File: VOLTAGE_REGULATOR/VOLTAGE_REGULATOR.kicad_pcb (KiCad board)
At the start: 2 copper layers, 13 parts, among them J1 Screw_Terminal_01x02, J2 Screw_Terminal_01x02, J3 Screw_Terminal_01x02, U1 L7805, U2 L7809

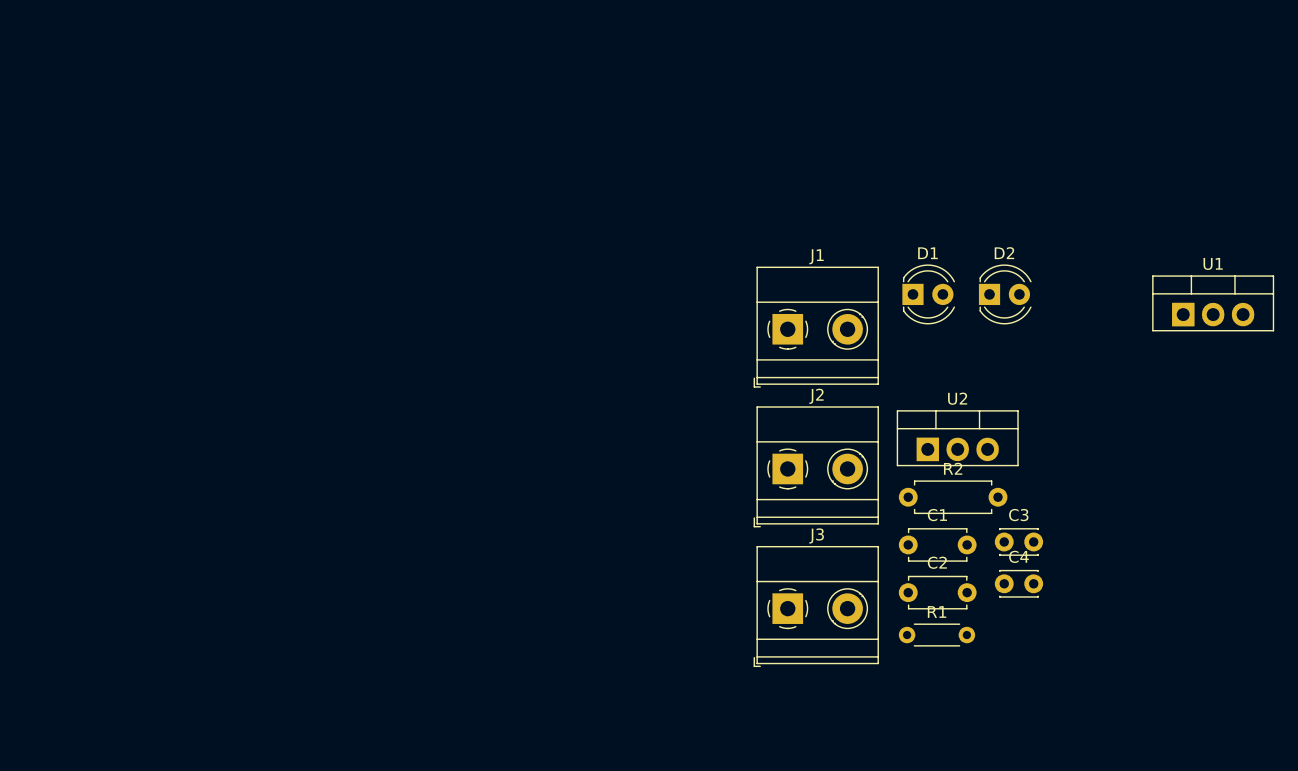
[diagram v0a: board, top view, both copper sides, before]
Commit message: voltage regulator: place components
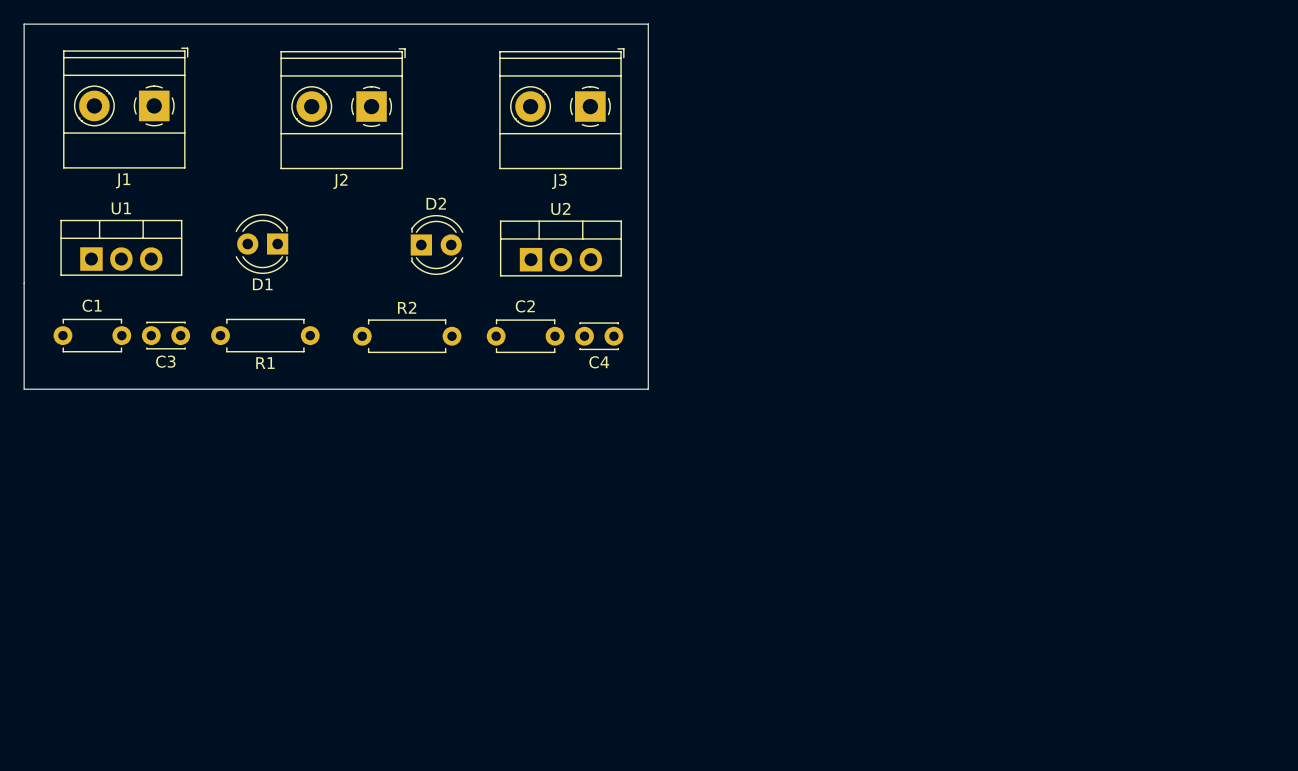
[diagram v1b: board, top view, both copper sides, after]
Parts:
- R1: footprint Resistor_THT:R_Axial_DIN0204_L3.6mm_D1.6mm_P5.08mm_Horizontal -> Resistor_THT:R_Axial_DIN0207_L6.3mm_D2.5mm_P7.62mm_Horizontal
- moved U1 92.8 mm to (92.7, 68.9)
- moved C1 73.9 mm to (90.3, 75.4)
- moved C3 72.1 mm to (100.3, 75.4), turned to 180 degrees
- moved J1 57.0 mm to (98.0, 55.9), turned to 180 degrees
- moved R1 56.7 mm to (111.3, 75.4), turned to 180 degrees
- moved D1 54.1 mm to (108.5, 67.7), turned to 180 degrees
- moved D2 48.4 mm to (120.7, 67.8)
- moved R2 48.3 mm to (115.7, 75.5)
- moved J2 46.9 mm to (116.5, 56.0), turned to 180 degrees
- moved J3 45.8 mm to (135.1, 56.0), turned to 180 degrees
- moved C2 41.2 mm to (127.1, 75.5)
- moved C4 39.2 mm to (137.1, 75.5), turned to 180 degrees
- moved U2 37.3 mm to (130.0, 69.0)
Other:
- board outline added: 53 x 31 mm

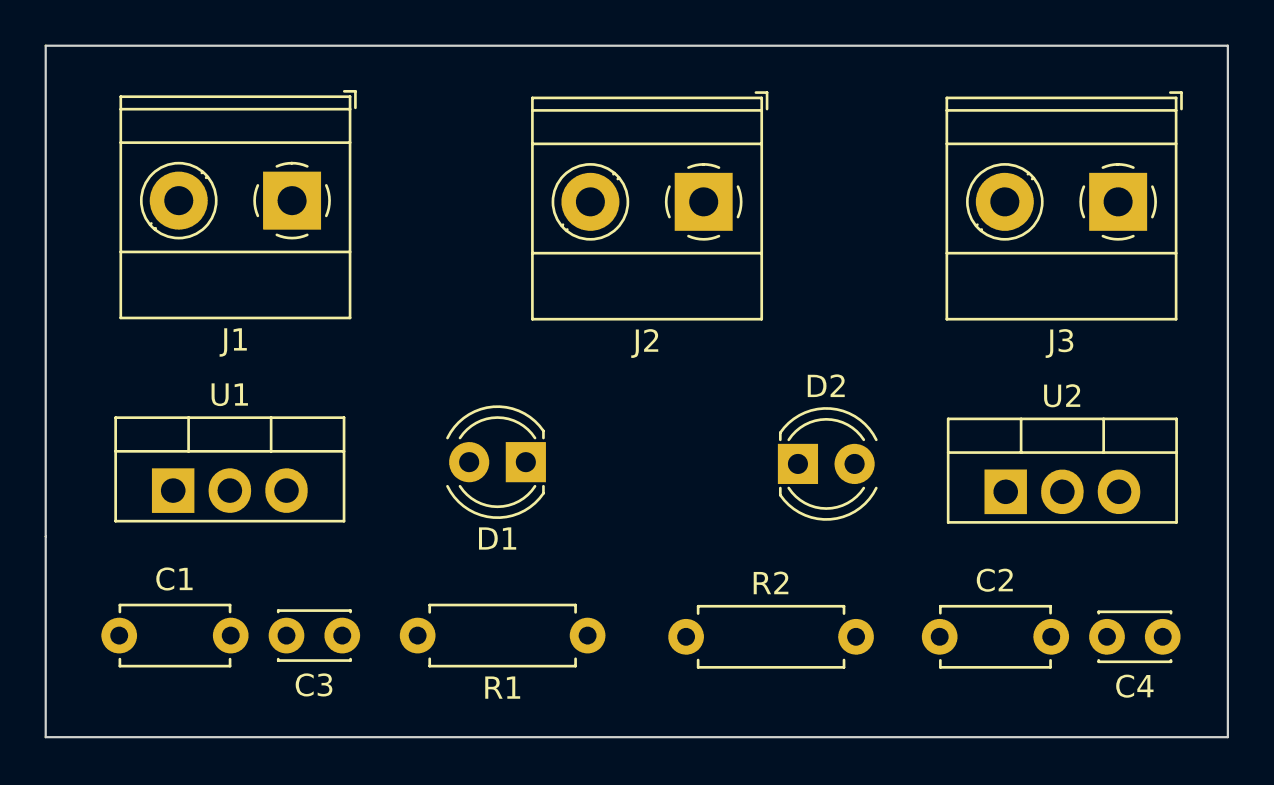
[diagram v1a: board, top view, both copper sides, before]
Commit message: route pcb main connections
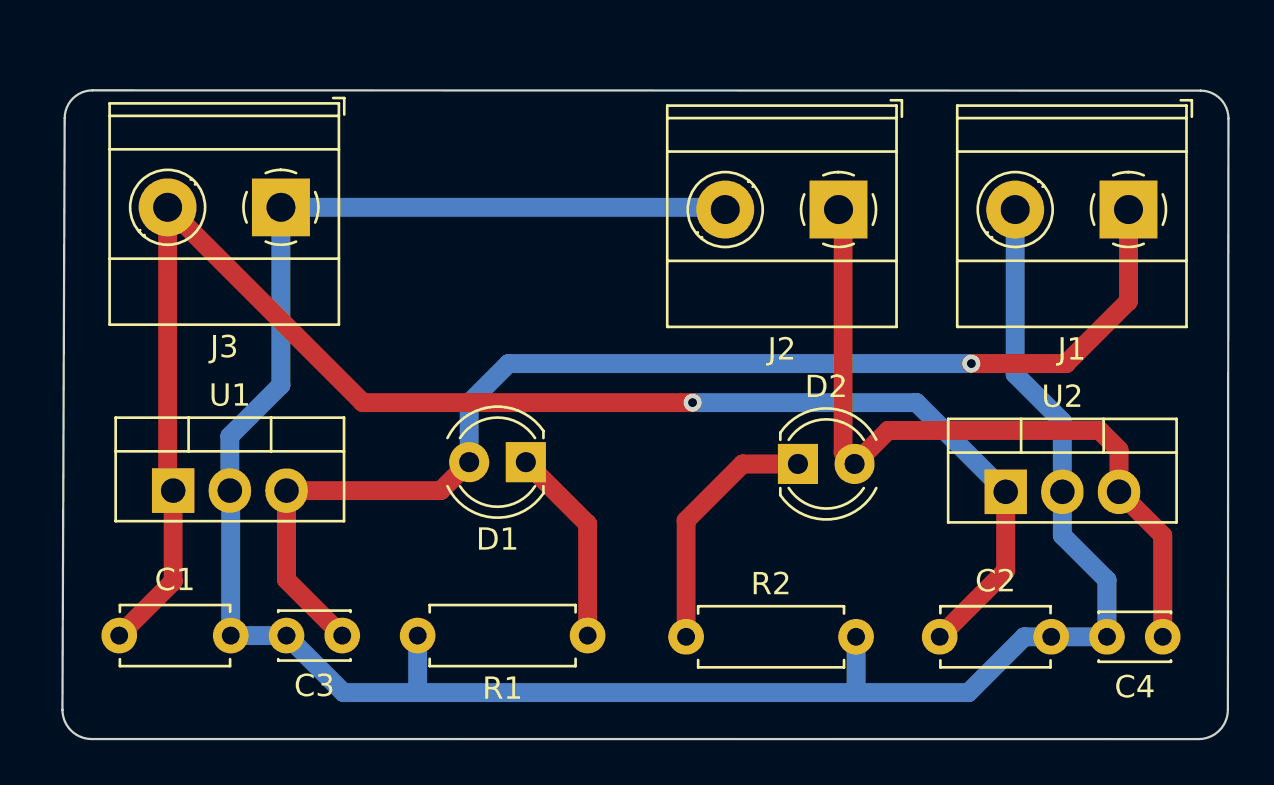
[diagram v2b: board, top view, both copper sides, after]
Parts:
- moved J3 37.5 mm to (97.5, 56.2)
- moved J1 37.5 mm to (135.5, 56.3)
- moved J2 6.05 mm to (122.5, 56.3)
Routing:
- net GND: track 0.00 -> 107.6 mm
- net +12V: track 0.00 -> 70.9 mm, vias 0 -> 1
- net /+5V_OUT: track 0.00 -> 54.5 mm, vias 0 -> 1
- net /+9V_OUT: track 0.00 -> 33.7 mm
- net Net-(D2-K): track 0.00 -> 11.3 mm
- net Net-(D1-K): track 0.00 -> 8.92 mm
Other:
- board size 53 x 31 mm -> 52.3 x 29.1 mm
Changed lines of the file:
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@@
   )
   (footprint "TerminalBlock_Phoenix:TerminalBlock_Phoenix_MKDS-1,5-2-5.08_1x02_P5.08mm_Horizontal" (layer "F.Cu")
-    (at 98.045 55.945 180)
+    (at 135.545 56.345 180)
     (descr "Terminal Block Phoenix MKDS-1,5-2-5.08, 2 pins, pitch 5.08mm, size 10.2x9.8mm^2, drill diamater 1.3mm, pad diameter 2.6mm, see http://www.farnell.com/datasheets/100425.pdf, script-generated using https://github.com/pointhi/kicad-footprint-generator/scripts/TerminalBlock_Phoenix")
     (tags "THT Terminal Block Phoenix MKDS-1,5-2-5.08 pitch 5.08mm size 10.2x9.8mm^2 drill 1.3mm pad 2.6mm")
@@
   )
   (footprint "TerminalBlock_Phoenix:TerminalBlock_Phoenix_MKDS-1,5-2-5.08_1x02_P5.08mm_Horizontal" (layer "F.Cu")
-    (at 135.08 56 180)
+    (at 97.545 56.245 180)
     (descr "Terminal Block Phoenix MKDS-1,5-2-5.08, 2 pins, pitch 5.08mm, size 10.2x9.8mm^2, drill diamater 1.3mm, pad diameter 2.6mm, see http://www.farnell.com/datasheets/100425.pdf, script-generated using https://github.com/pointhi/kicad-footprint-generator/scripts/TerminalBlock_Phoenix")
     (tags "THT Terminal Block Phoenix MKDS-1,5-2-5.08 pitch 5.08mm size 10.2x9.8mm^2 drill 1.3mm pad 2.6mm")
@@
   )
   (footprint "TerminalBlock_Phoenix:TerminalBlock_Phoenix_MKDS-1,5-2-5.08_1x02_P5.08mm_Horizontal" (layer "F.Cu")
-    (at 116.5 56 180)
+    (at 122.545 56.345 180)
     (descr "Terminal Block Phoenix MKDS-1,5-2-5.08, 2 pins, pitch 5.08mm, size 10.2x9.8mm^2, drill diamater 1.3mm, pad diameter 2.6mm, see http://www.farnell.com/datasheets/100425.pdf, script-generated using https://github.com/pointhi/kicad-footprint-generator/scripts/TerminalBlock_Phoenix")
     (tags "THT Terminal Block Phoenix MKDS-1,5-2-5.08 pitch 5.08mm size 10.2x9.8mm^2 drill 1.3mm pad 2.6mm")
@@
     )
   )
-  (gr_line (start 140 49) (end 140 80)
+  (gr_arc (start 138.776117 51.013883) (mid 139.66 51.38) (end 140.026117 52.263883)
     (stroke (width 0.1) (type default)) (layer "Edge.Cuts"))
-  (gr_line (start 140 80) (end 87 80)
+  (gr_line (start 138.776117 51.013883) (end 89.1 51)
     (stroke (width 0.1) (type default)) (layer "Edge.Cuts"))
-  (gr_line (start 87 80) (end 87 71)
+  (gr_line (start 87.85 52.25) (end 87.75 78.772888)
     (stroke (width 0.1) (type default)) (layer "Edge.Cuts"))
-  (gr_line (start 87 49) (end 140 49)
+  (gr_arc (start 89.061134 80.084022) (mid 88.134022 79.7) (end 87.75 78.772888)
     (stroke (width 0.1) (type default)) (layer "Edge.Cuts"))
-  (gr_line (start 87 71) (end 87 49)
+  (gr_line (start 89.061134 80.084022) (end 138.688866 80.086134)
     (stroke (width 0.1) (type default)) (layer "Edge.Cuts"))
+  (gr_arc (start 87.85 52.25) (mid 88.216117 51.366117) (end 89.1 51)
+    (stroke (width 0.1) (type default)) (layer "Edge.Cuts"))
+  (gr_arc (start 140.000034 78.775) (mid 139.616 79.702124) (end 138.688866 80.086134)
+    (stroke (width 0.1) (type default)) (layer "Edge.Cuts"))
+  (gr_line (start 140.000034 78.775) (end 140.026117 52.263883)
+    (stroke (width 0.1) (type default)) (layer "Edge.Cuts"))
+  (segment (start 92.465 56.245) (end 101.22 65) (width 0.85) (layer "F.Cu") (net 1))
+  (segment (start 92.715 68.945) (end 92.715 73.025) (width 0.85) (layer "F.Cu") (net 1))
+  (segment (start 101.22 65) (end 116 65) (width 0.85) (layer "F.Cu") (net 1))
+  (segment (start 92.715 73.025) (end 90.295 75.445) (width 0.85) (layer "F.Cu") (net 1))
+  (segment (start 130.04 72.54) (end 127.08 75.5) (width 0.85) (layer "F.Cu") (net 1))
+  (segment (start 92.465 68.695) (end 92.715 68.945) (width 0.85) (layer "F.Cu") (net 1))
+  (segment (start 92.465 56.245) (end 92.465 68.695) (width 0.85) (layer "F.Cu") (net 1))
+  (segment (start 130.04 69) (end 130.04 72.54) (width 0.85) (layer "F.Cu") (net 1))
+  (via (at 116 65) (size 0.8) (drill 0.4) (layers "F.Cu" "B.Cu") (net 1))
+  (segment (start 116 65) (end 126.04 65) (width 0.85) (layer "B.Cu") (net 1))
+  (segment (start 126.04 65) (end 130.04 69) (width 0.85) (layer "B.Cu") (net 1))
+  (segment (start 97.545 64.215) (end 97.545 56.245) (width 0.85) (layer "B.Cu") (net 2))
+  (segment (start 130.875 75.5) (end 128.375 78) (width 0.85) (layer "B.Cu") (net 2))
+  (segment (start 134.58 75.5) (end 132.08 75.5) (width 0.85) (layer "B.Cu") (net 2))
+  (segment (start 97.795 75.445) (end 95.295 75.445) (width 0.85) (layer "B.Cu") (net 2))
+  (segment (start 123.33 75.5) (end 123.33 77.795) (width 0.85) (layer "B.Cu") (net 2))
+  (segment (start 95.255 68.945) (end 95.255 66.505) (width 0.85) (layer "B.Cu") (net 2))
+  (segment (start 103.675 77.8) (end 103.875 78) (width 0.85) (layer "B.Cu") (net 2))
+  (segment (start 100.35 78) (end 97.795 75.445) (width 0.85) (layer "B.Cu") (net 2))
+  (segment (start 95.295 75.445) (end 95.295 68.985) (width 0.85) (layer "B.Cu") (net 2))
+  (segment (start 128.375 78) (end 123.125 78) (width 0.85) (layer "B.Cu") (net 2))
+  (segment (start 117.365 56.245) (end 117.465 56.345) (width 0.85) (layer "B.Cu") (net 2))
+  (segment (start 132.08 75.5) (end 130.875 75.5) (width 0.85) (layer "B.Cu") (net 2))
+  (segment (start 130.465 63.73) (end 130.465 56.345) (width 0.85) (layer "B.Cu") (net 2))
+  (segment (start 103.875 78) (end 100.35 78) (width 0.85) (layer "B.Cu") (net 2))
+  (segment (start 132.58 70.955) (end 134.58 72.955) (width 0.85) (layer "B.Cu") (net 2))
+  (segment (start 95.295 68.985) (end 95.255 68.945) (width 0.85) (layer "B.Cu") (net 2))
+  (segment (start 103.675 75.445) (end 103.675 77.8) (width 0.85) (layer "B.Cu") (net 2))
+  (segment (start 132.58 69) (end 132.58 70.955) (width 0.85) (layer "B.Cu") (net 2))
+  (segment (start 123.125 78) (end 103.875 78) (width 0.85) (layer "B.Cu") (net 2))
+  (segment (start 132.58 65.845) (end 132.58 69) (width 0.85) (layer "B.Cu") (net 2))
+  (segment (start 123.33 77.795) (end 123.125 78) (width 0.85) (layer "B.Cu") (net 2))
+  (segment (start 97.545 56.245) (end 117.365 56.245) (width 0.85) (layer "B.Cu") (net 2))
+  (segment (start 132.58 65.845) (end 130.465 63.73) (width 0.85) (layer "B.Cu") (net 2))
+  (segment (start 95.255 66.505) (end 97.545 64.215) (width 0.85) (layer "B.Cu") (net 2))
+  (segment (start 134.58 72.955) (end 134.58 75.5) (width 0.85) (layer "B.Cu") (net 2))
+  (segment (start 97.795 72.945) (end 100.295 75.445) (width 0.85) (layer "F.Cu") (net 3))
+  (segment (start 97.795 68.945) (end 104.71 68.945) (width 0.85) (layer "F.Cu") (net 3))
+  (segment (start 132.75 63.25) (end 135.545 60.455) (width 0.85) (layer "F.Cu") (net 3))
+  (segment (start 128.5 63.25) (end 132.75 63.25) (width 0.85) (layer "F.Cu") (net 3))
+  (segment (start 135.545 60.455) (end 135.545 56.345) (width 0.85) (layer "F.Cu") (net 3))
+  (segment (start 104.71 68.945) (end 105.985 67.67) (width 0.85) (layer "F.Cu") (net 3))
+  (segment (start 97.795 68.945) (end 97.795 72.945) (width 0.85) (layer "F.Cu") (net 3))
+  (via (at 128.5 63.25) (size 0.8) (drill 0.4) (layers "F.Cu" "B.Cu") (net 3))
+  (segment (start 105.985 67.67) (end 105.985 65.015) (width 0.85) (layer "B.Cu") (net 3))
+  (segment (start 107.75 63.25) (end 128.5 63.25) (width 0.85) (layer "B.Cu") (net 3))
+  (segment (start 105.985 65.015) (end 107.75 63.25) (width 0.85) (layer "B.Cu") (net 3))
+  (segment (start 123.265 67.75) (end 124.765 66.25) (width 0.85) (layer "F.Cu") (net 4))
+  (segment (start 122.75 56.55) (end 122.75 67.235) (width 0.85) (layer "F.Cu") (net 4))
+  (segment (start 137.08 75.5) (end 137.08 70.96) (width 0.85) (layer "F.Cu") (net 4))
+  (segment (start 134.25 66.25) (end 135.12 67.12) (width 0.85) (layer "F.Cu") (net 4))
+  (segment (start 137.08 70.96) (end 135.12 69) (width 0.85) (layer "F.Cu") (net 4))
+  (segment (start 122.545 56.345) (end 122.75 56.55) (width 0.85) (layer "F.Cu") (net 4))
+  (segment (start 124.765 66.25) (end 134.25 66.25) (width 0.85) (layer "F.Cu") (net 4))
+  (segment (start 122.75 67.235) (end 123.265 67.75) (width 0.85) (layer "F.Cu") (net 4))
+  (segment (start 135.12 67.12) (end 135.12 69) (width 0.85) (layer "F.Cu") (net 4))
+  (segment (start 111.295 70.44) (end 108.525 67.67) (width 0.85) (layer "F.Cu") (net 5))
+  (segment (start 111.295 75.445) (end 111.295 70.44) (width 0.85) (layer "F.Cu") (net 5))
+  (segment (start 120.725 67.75) (end 118.25 67.75) (width 0.85) (layer "F.Cu") (net 6))
+  (segment (start 118.25 67.75) (end 115.71 70.29) (width 0.85) (layer "F.Cu") (net 6))
+  (segment (start 115.71 70.29) (end 115.71 75.5) (width 0.85) (layer "F.Cu") (net 6))
 )

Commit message: voltage regulator: add fill zones
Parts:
- moved D2 54.5 mm to (166.0, 98.0)
- moved J1 54.5 mm to (180.9, 86.6)
- moved U2 54.5 mm to (175.4, 99.2)
- moved C1 54.5 mm to (135.6, 105.7)
- moved C2 54.5 mm to (172.4, 105.7)
- moved C3 54.5 mm to (145.6, 105.7)
- moved J2 54.5 mm to (167.9, 86.6)
- moved J3 54.5 mm to (142.9, 86.5)
- moved R1 54.5 mm to (156.6, 105.7)
- moved R2 54.5 mm to (161.0, 105.7)
- moved C4 54.5 mm to (182.4, 105.7)
- moved D1 54.5 mm to (153.8, 97.9)
- moved U1 54.5 mm to (138.0, 99.2)
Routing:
- added copper zone on B.Cu, net GND
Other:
- outline, holes or cut-outs redrawn
- board text added: "Voltage Regulator 5 and 9 Volts"
